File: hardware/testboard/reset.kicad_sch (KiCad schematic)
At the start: 8 parts, among them SW2 Button, U22 74LVC1G08, U23 TL7705A

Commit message: pinouts
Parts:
- renumbered C74 to C901, C75 to C902, C73 to C903, R25 to R901, R24 to R902, SW2 to SW901, U23 to U901, U22 to U902
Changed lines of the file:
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@@
   (symbol (lib_id "Device:C") (at 134.62 80.01 0) (mirror y) (unit 1)
     (in_bom yes) (on_board yes) (dnp no) (fields_autoplaced)
-    (property "Reference" "C75" (at 138.43 78.74 0)
+    (property "Reference" "C902" (at 138.43 78.74 0)
       (effects (font (size 1.27 1.27)) (justify right))
     )
@@
       (project "testboard"
         (path "/a1ce156a-fb78-423b-b05a-d07384e5c8a7/ed13931f-56ea-4f95-b129-e0c6d78034e8"
-          (reference "C75") (unit 1)
+          (reference "C902") (unit 1)
         )
       )
@@
   (symbol (lib_id "Power_Supervisor:TL7705A") (at 116.84 68.58 0) (unit 1)
     (in_bom yes) (on_board yes) (dnp no) (fields_autoplaced)
-    (property "Reference" "U23" (at 119.0341 55.88 0)
+    (property "Reference" "U901" (at 119.0341 55.88 0)
       (effects (font (size 1.27 1.27)) (justify left))
     )
@@
       (project "testboard"
         (path "/a1ce156a-fb78-423b-b05a-d07384e5c8a7/ed13931f-56ea-4f95-b129-e0c6d78034e8"
-          (reference "U23") (unit 1)
+          (reference "U901") (unit 1)
         )
       )
@@
   (symbol (lib_id "power:GND") (at 205.74 45.72 0) (unit 1)
     (in_bom yes) (on_board yes) (dnp no) (fields_autoplaced)
-    (property "Reference" "#PWR0141" (at 205.74 52.07 0)
+    (property "Reference" "#PWR0907" (at 205.74 52.07 0)
       (effects (font (size 1.27 1.27)) hide)
     )
@@
       (project "testboard"
         (path "/a1ce156a-fb78-423b-b05a-d07384e5c8a7/ed13931f-56ea-4f95-b129-e0c6d78034e8"
-          (reference "#PWR0141") (unit 1)
+          (reference "#PWR0907") (unit 1)
         )
       )
@@
   (symbol (lib_id "74xGxx:74LVC1G08") (at 185.42 60.96 0) (unit 1)
     (in_bom yes) (on_board yes) (dnp no) (fields_autoplaced)
-    (property "Reference" "U22" (at 196.85 56.7691 0)
+    (property "Reference" "U902" (at 196.85 56.7691 0)
       (effects (font (size 1.27 1.27)))
     )
@@
       (project "testboard"
         (path "/a1ce156a-fb78-423b-b05a-d07384e5c8a7/ed13931f-56ea-4f95-b129-e0c6d78034e8"
-          (reference "U22") (unit 1)
+          (reference "U902") (unit 1)
         )
       )
@@
   (symbol (lib_id "Device:R_Small_US") (at 139.7 58.42 0) (unit 1)
     (in_bom yes) (on_board yes) (dnp no)
-    (property "Reference" "R24" (at 137.16 57.15 0)
+    (property "Reference" "R902" (at 137.16 57.15 0)
       (effects (font (size 1.27 1.27)) (justify right))
     )
@@
       (project "testboard"
         (path "/a1ce156a-fb78-423b-b05a-d07384e5c8a7/ed13931f-56ea-4f95-b129-e0c6d78034e8"
-          (reference "R24") (unit 1)
+          (reference "R902") (unit 1)
         )
       )
@@
   (symbol (lib_id "Device:C") (at 99.06 80.01 0) (mirror y) (unit 1)
     (in_bom yes) (on_board yes) (dnp no) (fields_autoplaced)
-    (property "Reference" "C74" (at 102.87 78.74 0)
+    (property "Reference" "C901" (at 102.87 78.74 0)
       (effects (font (size 1.27 1.27)) (justify right))
     )
@@
       (project "testboard"
         (path "/a1ce156a-fb78-423b-b05a-d07384e5c8a7/ed13931f-56ea-4f95-b129-e0c6d78034e8"
-          (reference "C74") (unit 1)
+          (reference "C901") (unit 1)
         )
       )
@@
   (symbol (lib_id "power:+5V") (at 185.42 50.8 0) (unit 1)
     (in_bom yes) (on_board yes) (dnp no) (fields_autoplaced)
-    (property "Reference" "#PWR0138" (at 185.42 54.61 0)
+    (property "Reference" "#PWR0904" (at 185.42 54.61 0)
       (effects (font (size 1.27 1.27)) hide)
     )
@@
       (project "testboard"
         (path "/a1ce156a-fb78-423b-b05a-d07384e5c8a7/ed13931f-56ea-4f95-b129-e0c6d78034e8"
-          (reference "#PWR0138") (unit 1)
+          (reference "#PWR0904") (unit 1)
         )
       )
@@
   (symbol (lib_id "power:GND") (at 63.5 71.12 0) (unit 1)
     (in_bom yes) (on_board yes) (dnp no) (fields_autoplaced)
-    (property "Reference" "#PWR0136" (at 63.5 77.47 0)
+    (property "Reference" "#PWR0901" (at 63.5 77.47 0)
       (effects (font (size 1.27 1.27)) hide)
     )
@@
       (project "testboard"
         (path "/a1ce156a-fb78-423b-b05a-d07384e5c8a7/ed13931f-56ea-4f95-b129-e0c6d78034e8"
-          (reference "#PWR0136") (unit 1)
+          (reference "#PWR0901") (unit 1)
         )
       )
@@
   (symbol (lib_id "Switch:SW_Push") (at 73.66 68.58 0) (unit 1)
     (in_bom yes) (on_board yes) (dnp no) (fields_autoplaced)
-    (property "Reference" "SW2" (at 73.66 60.96 0)
+    (property "Reference" "SW901" (at 73.66 60.96 0)
       (effects (font (size 1.27 1.27)))
     )
@@
       (project "testboard"
         (path "/a1ce156a-fb78-423b-b05a-d07384e5c8a7/ed13931f-56ea-4f95-b129-e0c6d78034e8"
-          (reference "SW2") (unit 1)
+          (reference "SW901") (unit 1)
         )
       )
@@
   (symbol (lib_id "power:GND") (at 116.84 86.36 0) (unit 1)
     (in_bom yes) (on_board yes) (dnp no) (fields_autoplaced)
-    (property "Reference" "#PWR0137" (at 116.84 92.71 0)
+    (property "Reference" "#PWR0903" (at 116.84 92.71 0)
       (effects (font (size 1.27 1.27)) hide)
     )
@@
       (project "testboard"
         (path "/a1ce156a-fb78-423b-b05a-d07384e5c8a7/ed13931f-56ea-4f95-b129-e0c6d78034e8"
-          (reference "#PWR0137") (unit 1)
+          (reference "#PWR0903") (unit 1)
         )
       )
@@
   (symbol (lib_id "Device:C") (at 205.74 41.91 0) (mirror y) (unit 1)
     (in_bom yes) (on_board yes) (dnp no) (fields_autoplaced)
-    (property "Reference" "C73" (at 209.55 40.64 0)
+    (property "Reference" "C903" (at 209.55 40.64 0)
       (effects (font (size 1.27 1.27)) (justify right))
     )
@@
       (project "testboard"
         (path "/a1ce156a-fb78-423b-b05a-d07384e5c8a7/ed13931f-56ea-4f95-b129-e0c6d78034e8"
-          (reference "C73") (unit 1)
+          (reference "C903") (unit 1)
         )
       )
@@
   (symbol (lib_id "power:GND") (at 185.42 71.12 0) (unit 1)
     (in_bom yes) (on_board yes) (dnp no) (fields_autoplaced)
-    (property "Reference" "#PWR0139" (at 185.42 77.47 0)
+    (property "Reference" "#PWR0905" (at 185.42 77.47 0)
       (effects (font (size 1.27 1.27)) hide)
     )
@@
       (project "testboard"
         (path "/a1ce156a-fb78-423b-b05a-d07384e5c8a7/ed13931f-56ea-4f95-b129-e0c6d78034e8"
-          (reference "#PWR0139") (unit 1)
+          (reference "#PWR0905") (unit 1)
         )
       )
@@
   (symbol (lib_id "Device:R_Small_US") (at 99.06 66.04 0) (unit 1)
     (in_bom yes) (on_board yes) (dnp no)
-    (property "Reference" "R25" (at 96.52 64.77 0)
+    (property "Reference" "R901" (at 96.52 64.77 0)
       (effects (font (size 1.27 1.27)) (justify right))
     )
@@
       (project "testboard"
         (path "/a1ce156a-fb78-423b-b05a-d07384e5c8a7/ed13931f-56ea-4f95-b129-e0c6d78034e8"
-          (reference "R25") (unit 1)
+          (reference "R901") (unit 1)
         )
       )
@@
   (symbol (lib_id "power:+5V") (at 205.74 38.1 0) (unit 1)
     (in_bom yes) (on_board yes) (dnp no) (fields_autoplaced)
-    (property "Reference" "#PWR0140" (at 205.74 41.91 0)
+    (property "Reference" "#PWR0906" (at 205.74 41.91 0)
       (effects (font (size 1.27 1.27)) hide)
     )
@@
       (project "testboard"
         (path "/a1ce156a-fb78-423b-b05a-d07384e5c8a7/ed13931f-56ea-4f95-b129-e0c6d78034e8"
-          (reference "#PWR0140") (unit 1)
+          (reference "#PWR0906") (unit 1)
         )
       )
@@
   (symbol (lib_id "power:+5V") (at 116.84 48.26 0) (unit 1)
     (in_bom yes) (on_board yes) (dnp no) (fields_autoplaced)
-    (property "Reference" "#PWR056" (at 116.84 52.07 0)
+    (property "Reference" "#PWR0902" (at 116.84 52.07 0)
       (effects (font (size 1.27 1.27)) hide)
     )
@@
       (project "testboard"
         (path "/a1ce156a-fb78-423b-b05a-d07384e5c8a7/ed13931f-56ea-4f95-b129-e0c6d78034e8"
-          (reference "#PWR056") (unit 1)
-        )
-      )
+          (reference "#PWR0902") (unit 1)
+        )
+      )

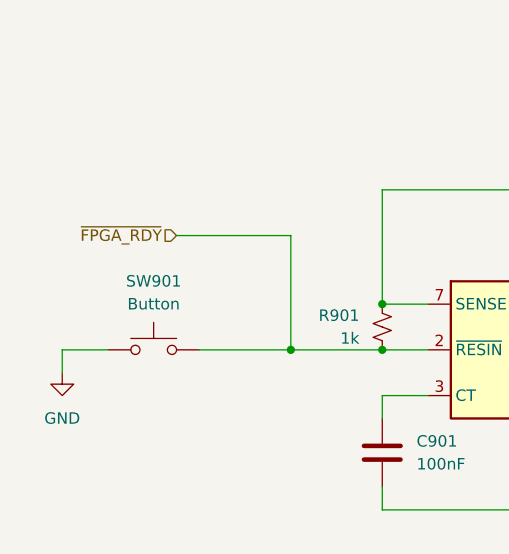
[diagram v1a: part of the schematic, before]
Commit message: testboard - schematic and route done
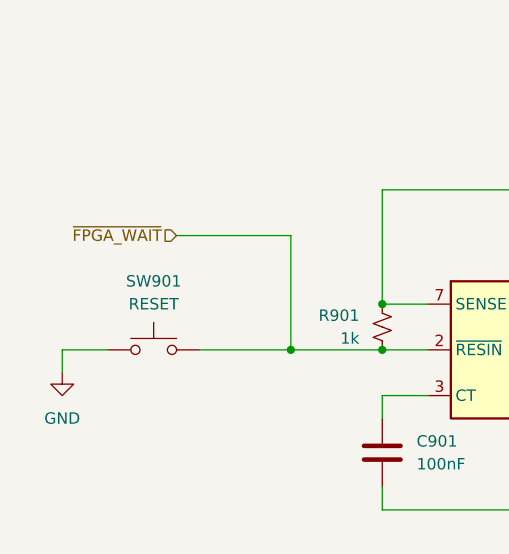
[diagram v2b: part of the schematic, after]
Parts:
- SW901: value Button -> RESET
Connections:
- net ~{FPGA_RDY} renamed ~{FPGA_WAIT}
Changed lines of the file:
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@@
     (effects (font (size 1.27 1.27)) (justify left))
   )
-  (hierarchical_label "~{FPGA_RDY}" (shape input) (at 76.2 55.88 180) (fields_autoplaced)
+  (hierarchical_label "~{FPGA_WAIT}" (shape input) (at 76.2 55.88 180) (fields_autoplaced)
     (effects (font (size 1.27 1.27)) (justify right))
   )
@@
       (effects (font (size 1.27 1.27)))
     )
-    (property "Value" "Button" (at 73.66 63.5 0)
-      (effects (font (size 1.27 1.27)))
-    )
+    (property "Value" "RESET" (at 73.66 63.5 0)
+      (effects (font (size 1.27 1.27)))
+    )
